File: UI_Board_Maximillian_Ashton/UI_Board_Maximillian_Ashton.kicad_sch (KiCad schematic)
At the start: 50 parts, among them J1 22035035, J2 XT60-M, SW1 A8L-11-12N1, U4 MCP2562-E-P, U6 TPS7A2030PDBVR, U7 CD4511BPWR

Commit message: Updated schematic. Should have resolved all comments
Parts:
- removed R11: R_Variable_US, symbol Device:R_Variable_US
- added C9: 0.10 uF, 50 V, symbol Device:C
- added J3: 22035035, SMV_Connectors:3pin_CON_22035035_MOL, symbol SMV_Custom:3-pin Mini Molex Spox
- added J4: XT60-M, SMV_Connectors:AMASS_XT60-M, symbol SMV_Custom:XT60-M
- added Q1, Q2, Q3, Q4: 2N3904, Package_TO_SOT_THT:TO-92_Inline, symbol Transistor_BJT:2N3904
- added R11, R21, R22, R25: 1K ohms, 0.125 watts, symbol Device:R_US
- added R20, R23, R24, R26: 100 ohms, 0.125 watts, symbol Device:R_US
- added RV1: 10K ohms, 0.125 Watts, symbol Device:R_Potentiometer_Trim_US
- added TP4, TP5, TP6, TP7: TestPoint, symbol Connector:TestPoint
- C1: value C -> 0.33 uF, 50 V
- C2, C5, C6, C7, C8: value C -> 0.10 uF, 50 V
- C3, C4: value C -> 0.10 uF, 50V
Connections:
- net +12V: now also J4.P (POS)
- net +3.3V: now also U1.5 (VDD), C9.2
- net +3V0: now also U5. (DB7), RV1.1, TP7.1
- net +5V: now also U1.6 (E5V), TP6.1; no longer U1.18 (+5V)
- net Digit 1: now also R25.2; no longer U2.12 (DIGIT_1)
- net Digit 2: now also R21.2; no longer U2.8 (DIGIT_2)
- net Digit 3: now also R22.2; no longer U2.7 (DIGIT_3)
- net Digit 4: now also R11.2; no longer U2.3 (DIGIT_4)
- net GND: now also U1.47 (GND), U1.58 (GND), U1.8 (GND), C9.1, J3.2, J4.N (NEG), R20.2, R23.2, R24.1, R26.2, RV1.3
- net CANH: now reaches J1.1, U4.7 (CANH)
- net CANH: now also J3.1, TP5.1
- net CANL: now reaches J1.3, U4.6 (CANL)
- net CANL: now also J3.3, TP4.1
- net V0 LCD: now reaches U5. (DB7)
- net V0 LCD: now also RV1.2
- new net: Q2.1 (E), R24.2
- new net: Q4.3 (C), U2.12 (DIGIT_1)
- new net: Q1.3 (C), U2.3 (DIGIT_4)
- new net: Q2.3 (C), U2.7 (DIGIT_3)
- new net: Q3.3 (C), U2.8 (DIGIT_2)
- new net: Q1.1 (E), R20.1
- new net: Q1.2 (B), R11.1
- new net: Q2.2 (B), R22.1
- new net: Q3.1 (E), R23.1
- new net: Q3.2 (B), R21.1
- new net: Q4.2 (B), R25.1
- new net: Q4.1 (E), R26.1
- no-connect marks 5 -> 40
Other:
- moved on the sheet: A1, C1, C2, C8, J1, U5

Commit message: Updated from final comments
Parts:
- added R27, R28, R29, R30, R31, R32, R33, R34: 0 Ohms, 0.125 watts, symbol Device:R_US
- added TP8, TP9: TestPoint, symbol Connector:TestPoint
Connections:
- net A: now also R32.1; no longer U2.9 (A)
- net B: now also R27.2; no longer U2.6 (B)
- net C: now also R29.2; no longer U2.4 (C)
- net CAN RXD: now also TP9.1
- net CAN TXD: now also TP8.1
- net D: now also R30.2; no longer U2.2 (D)
- net DB7: no longer U5. (DB7)
- net DP: now also R28.2; no longer U2.5 (DP)
- net E: now also R31.2; no longer U1.72 (PC4), U2.1 (E), U5. (DB7)
- net F: now also R33.1; no longer U2.10 (F)
- net G: now also R34.1; no longer U2.11 (G)
- net Supercaps: now reaches U1.1 (PC10)
- net Supercaps: now also B2.1, R6.1
- net Regen: now reaches U1.39 (PC9)
- net Regen: now also R19.2, S6.1 (Top)
- removed net Extra: B2.1, R19.2, R6.1, S6.1 (Top)
- new net: R34.2, U2.11 (G)
- new net: R31.1, U2.1 (E)
- new net: R33.2, U2.10 (F)
- new net: R30.1, U2.2 (D)
- new net: R29.1, U2.4 (C)
- new net: R28.1, U2.5 (DP)
- new net: R27.1, U2.6 (B)
- new net: R32.2, U2.9 (A)
- new net DB&7: U5. (DB7)
- new net E LCD: U1.72 (PC4), U5. (DB7)
- no-connect marks 40 -> 61
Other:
- moved on the sheet: C7, J1, J3, R12, R13, R14, R15, R16, R17, R18, U7

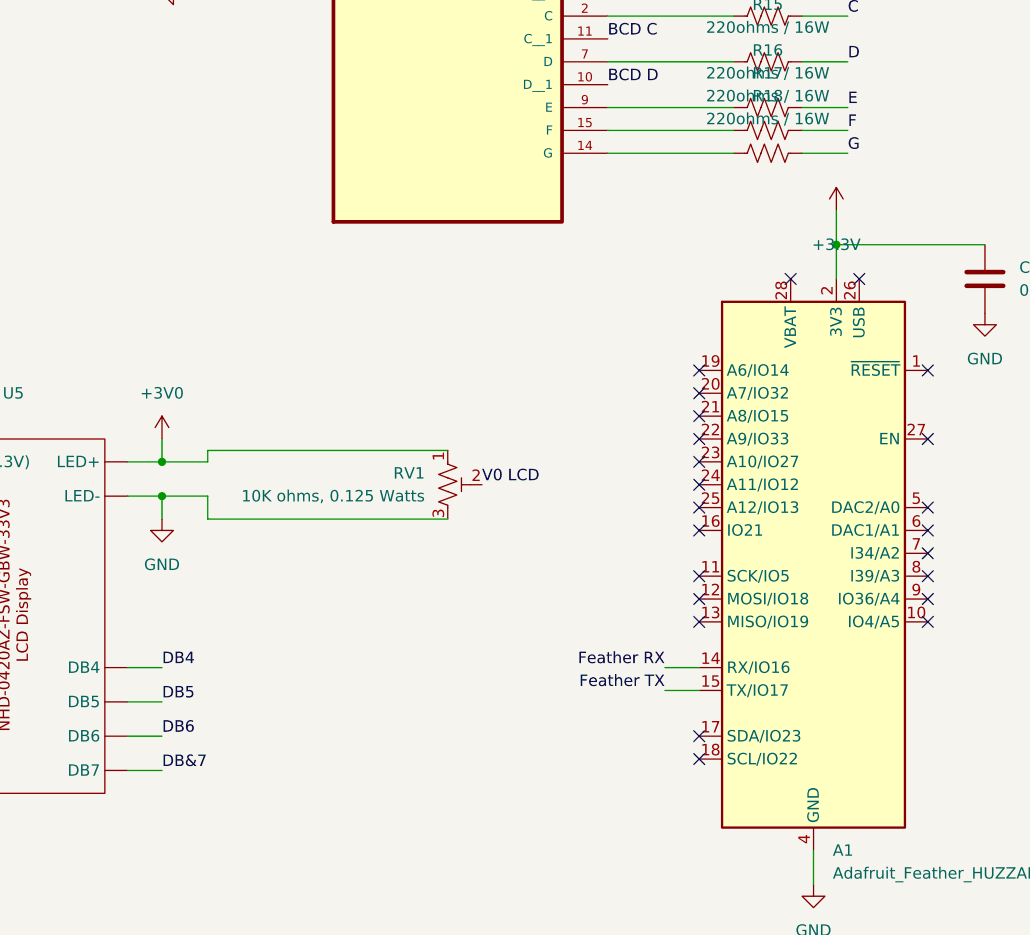
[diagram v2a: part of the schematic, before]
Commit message: Here is my latest draft of the layout. Please review the connections for the multiplexer. I was looking at the datasheet and found that it was wired incorrectly.
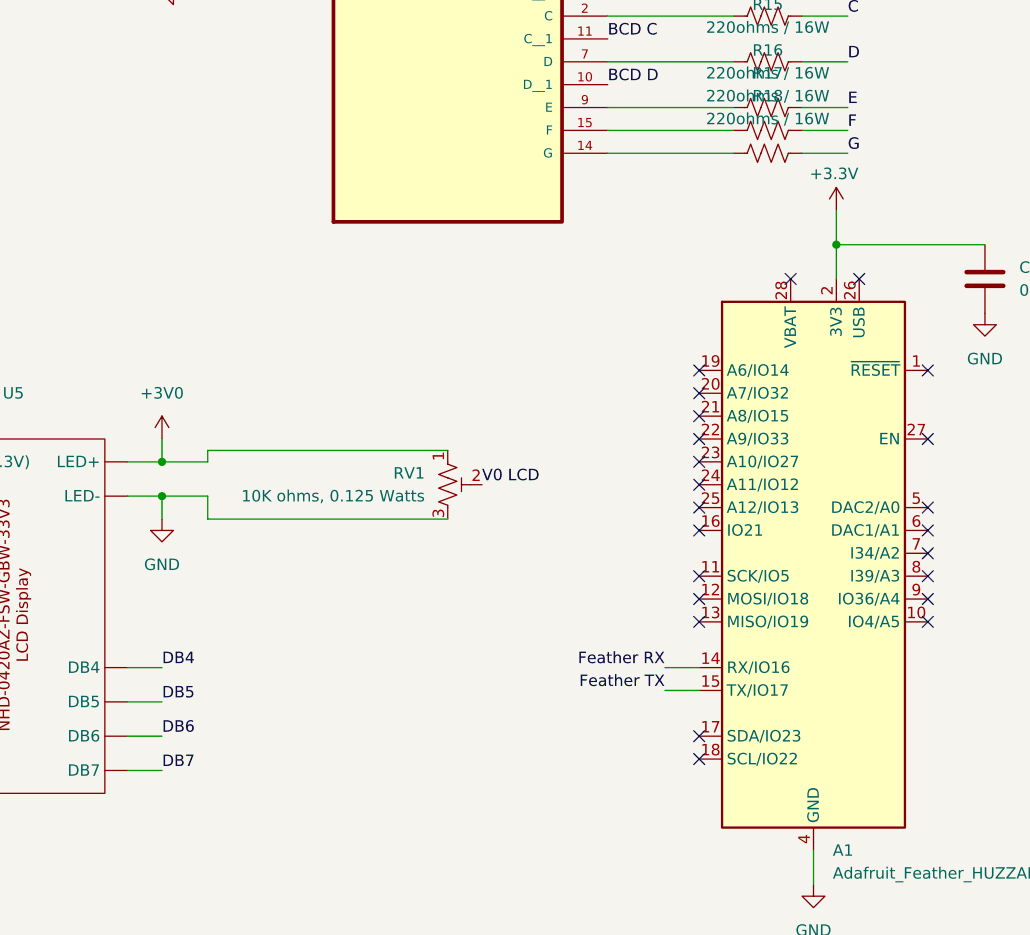
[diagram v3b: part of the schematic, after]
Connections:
- net DB&7 is gone; now on net V0 LCD: U5. (DB7)
- net DB7: now also U5. (DB7)
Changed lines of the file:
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@@
 		)
 	)
-	(label "DB&7"
+	(label "DB7"
 		(at 163.83 198.12 0)
 		(effects
@@
 		)
 		(property "Value" "+3.3V"
-			(at 238.76 139.7 0)
+			(at 238.506 131.826 0)
 			(effects
 				(font
